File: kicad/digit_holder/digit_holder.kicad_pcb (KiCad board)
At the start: 2 copper layers, 25.4 x 31.8 mm, 3 parts, among them J1 Conn_01x07_Male, J2 Conn_01x08_Male

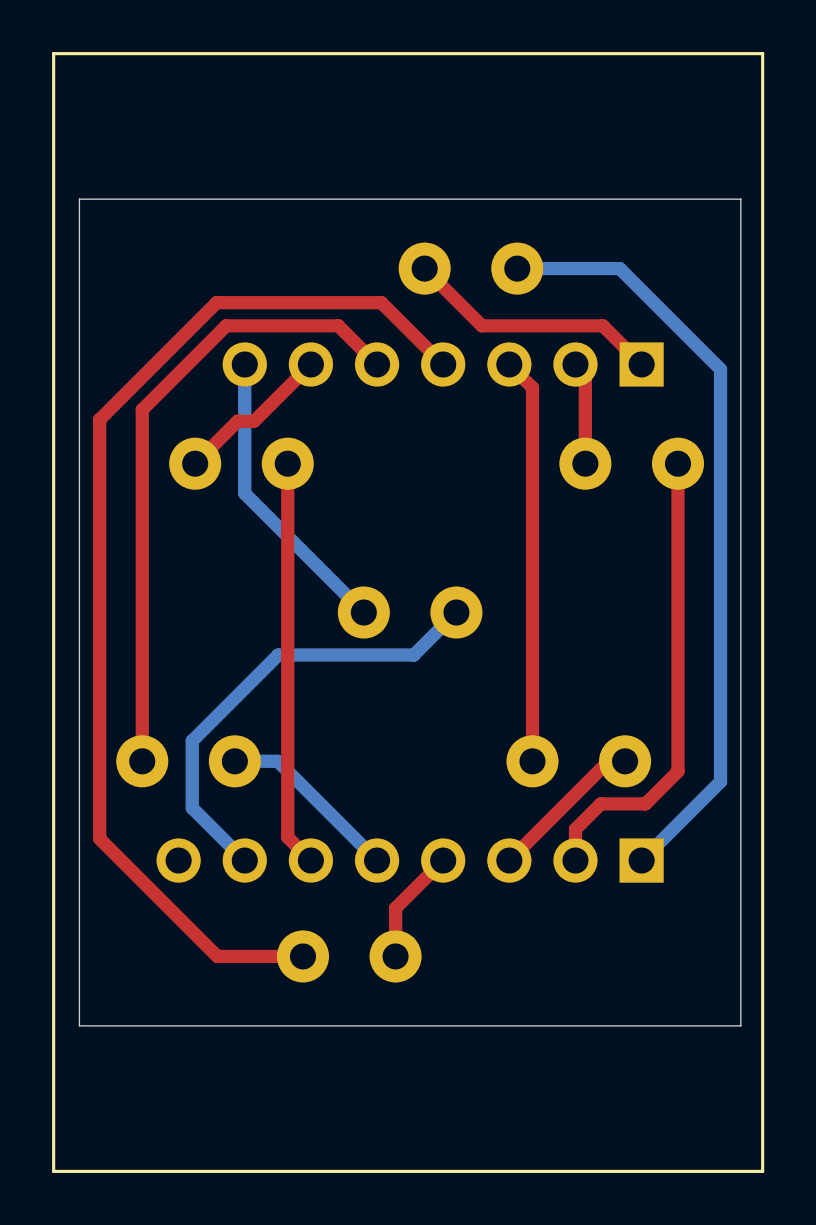
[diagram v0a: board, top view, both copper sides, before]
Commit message: add digit holder ground planes
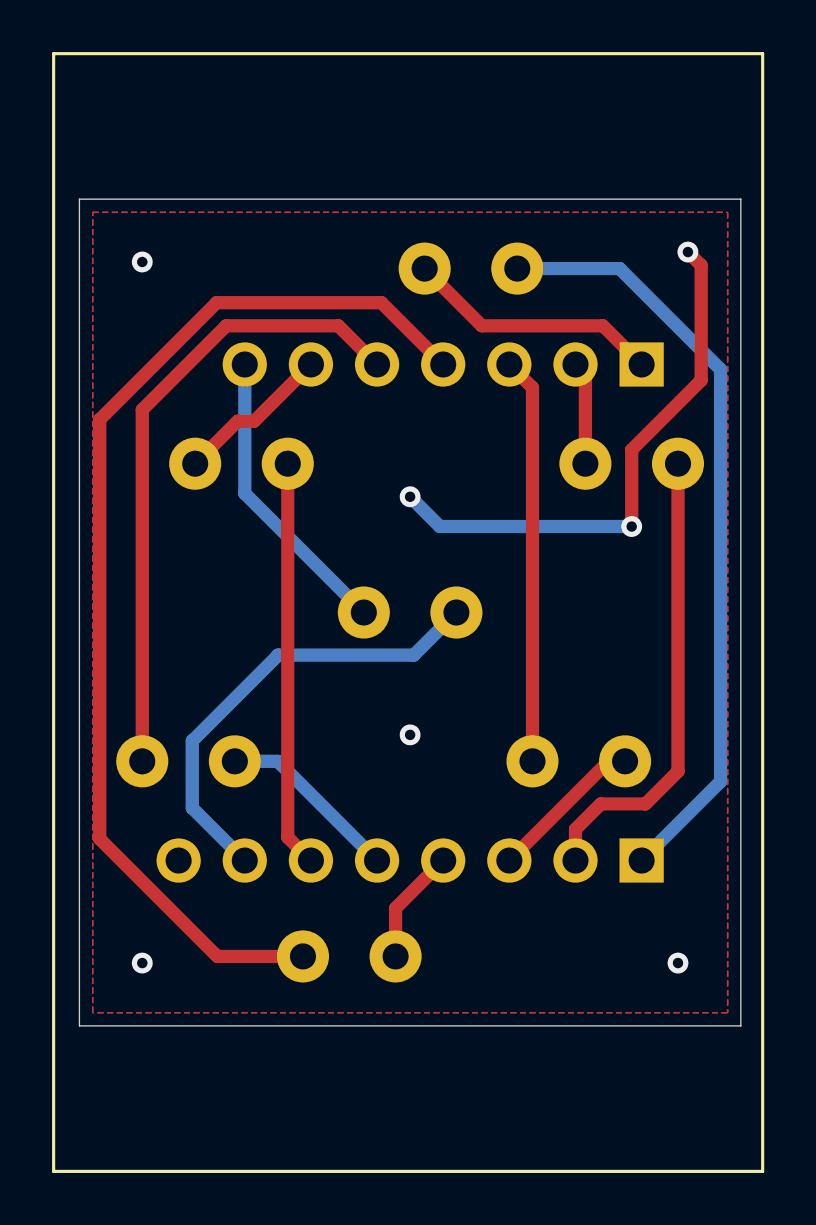
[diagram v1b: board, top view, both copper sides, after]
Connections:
- net Net-(J2-Pad8) renamed GND
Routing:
- net GND: track 0.00 -> 20.8 mm, vias 0 -> 7
- added copper zone on B.Cu, net GND
- added copper zone on F.Cu, net GND
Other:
- net class Default removed

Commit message: dfm
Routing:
- net GND: track 20.8 -> 0.00 mm, vias 7 -> 9
- net Net-(DS1-D_SET): track 41.8 -> 42.4 mm
